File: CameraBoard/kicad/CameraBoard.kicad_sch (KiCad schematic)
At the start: 0 parts

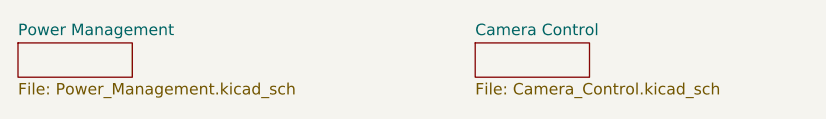
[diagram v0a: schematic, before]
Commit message: Updated KiCAD EAGLE import to latest KiCAD 9.0.2.
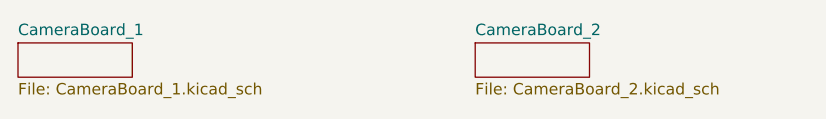
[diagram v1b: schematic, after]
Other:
- removed sheet Camera Control
- removed sheet Power Management
- added sheet CameraBoard_1 (CameraBoard_1.kicad_sch)
- added sheet CameraBoard_2 (CameraBoard_2.kicad_sch)
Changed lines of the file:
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@@
-(kicad_sch (version 20230121) (generator eeschema)
-  (paper "A4")
-  (sheet (at 76.2 25.4) (size 12.7 3.81) (fields_autoplaced)
-    (stroke (width 0) (type solid))
-    (fill (color 0 0 0 0.0000))
-    (property "Sheetname" "Camera Control" (at 76.2 24.6884 0)
-      (effects (font (size 1.27 1.27)) (justify left bottom))
-    )
-    (property "Sheetfile" "Camera_Control.kicad_sch" (at 76.2 29.7946 0)
-      (effects (font (size 1.27 1.27)) (justify left top))
-    )
-    (instances
-      (project "CameraBoard"
-        (path "/ff754bbd-8142-444b-bfb6-09e5bcbc7539" (page "2"))
-      )
-    )
-  )
-  (sheet (at 25.4 25.4) (size 12.7 3.81) (fields_autoplaced)
-    (stroke (width 0) (type solid))
-    (fill (color 0 0 0 0.0000))
-    (property "Sheetname" "Power Management" (at 25.4 24.6884 0)
-      (effects (font (size 1.27 1.27)) (justify left bottom))
-    )
-    (property "Sheetfile" "Power_Management.kicad_sch" (at 25.4 29.7946 0)
-      (effects (font (size 1.27 1.27)) (justify left top))
-    )
-    (instances
-      (project "CameraBoard"
-        (path "/ff754bbd-8142-444b-bfb6-09e5bcbc7539" (page "1"))
-      )
-    )
-  )
-  (sheet_instances
-    (path "/" (page "1"))
-  )
+(kicad_sch
+	(version 20250114)
+	(generator "eeschema")
+	(generator_version "9.0")
+	(paper "A4")
+	(sheet
+		(at 76.2 25.4)
+		(size 12.7 3.81)
+		(exclude_from_sim no)
+		(in_bom yes)
+		(on_board yes)
+		(dnp no)
+		(fields_autoplaced yes)
+		(stroke
+			(width 0)
+			(type solid)
+		)
+		(fill
+			(color 0 0 0 0.0000)
+		)
+		(property "Sheetname" "CameraBoard_2"
+			(at 76.2 24.6884 0)
+			(effects
+				(font
+					(size 1.27 1.27)
+				)
+				(justify left bottom)
+			)
+		)
+		(property "Sheetfile" "CameraBoard_2.kicad_sch"
+			(at 76.2 29.7946 0)
+			(effects
+				(font
+					(size 1.27 1.27)
+				)
+				(justify left top)
+			)
+		)
+		(instances
+			(project "CameraBoard"
+				(path "/876601fa-fbd1-4e2d-9c28-84441865735b"
+					(page "2")
+				)
+			)
+		)
+	)
+	(sheet
+		(at 25.4 25.4)
+		(size 12.7 3.81)
+		(exclude_from_sim no)
+		(in_bom yes)
+		(on_board yes)
+		(dnp no)
+		(fields_autoplaced yes)
+		(stroke
+			(width 0)
+			(type solid)
+		)
+		(fill
+			(color 0 0 0 0.0000)
+		)
+		(property "Sheetname" "CameraBoard_1"
+			(at 25.4 24.6884 0)
+			(effects
+				(font
+					(size 1.27 1.27)
+				)
+				(justify left bottom)
+			)
+		)
+		(property "Sheetfile" "CameraBoard_1.kicad_sch"
+			(at 25.4 29.7946 0)
+			(effects
+				(font
+					(size 1.27 1.27)
+				)
+				(justify left top)
+			)
+		)
+		(instances
+			(project "CameraBoard"
+				(path "/876601fa-fbd1-4e2d-9c28-84441865735b"
+					(page "1")
+				)
+			)
+		)
+	)
+	(sheet_instances
+		(path "/"
+			(page "1")
+		)
+	)
+	(embedded_fonts no)
 )
